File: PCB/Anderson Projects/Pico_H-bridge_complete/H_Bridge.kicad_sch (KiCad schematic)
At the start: 33 parts, among them Q1 AO3400A, Q2 AO3400A, Q3 DMP3130LQ-7, Q4 DMP3130LQ-7, U10 SN74LVC1G14DBV, U11 SN74LVC1G14DBV, U12 SN74LVC1G32, U13 SN74LVC1G32, U14 ILD217T, U15 ILD217T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

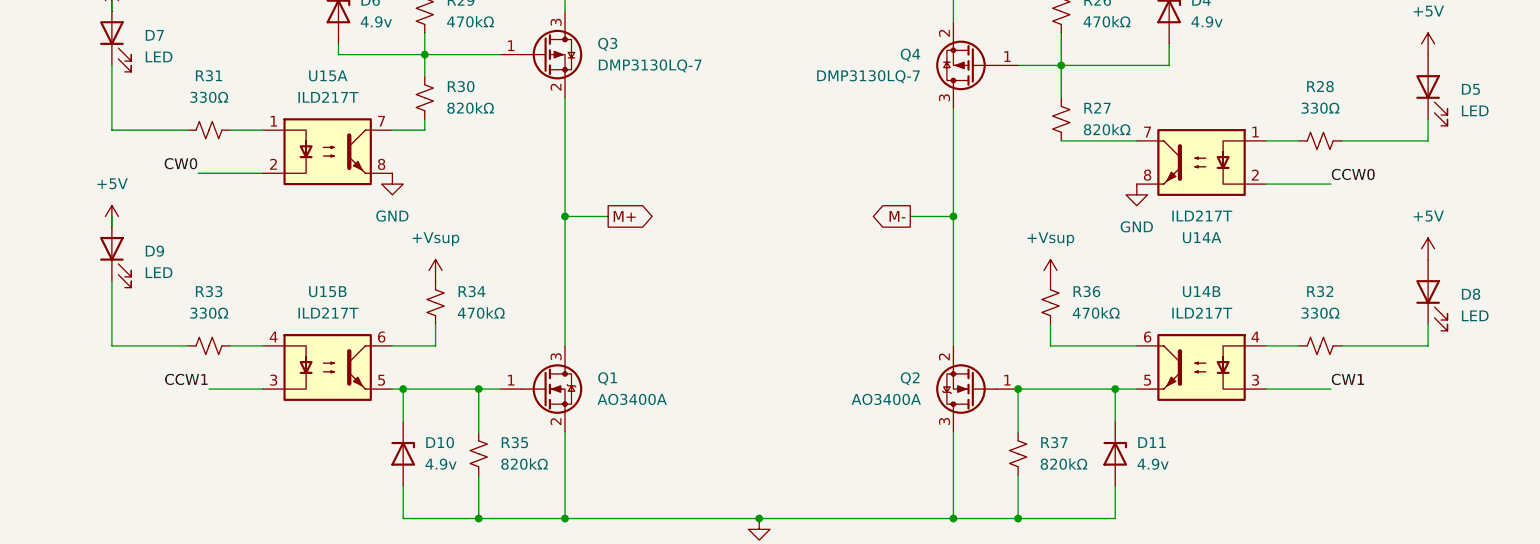
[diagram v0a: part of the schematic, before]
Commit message: Anderson Schematic with opto-couples prior to change to zener diodes
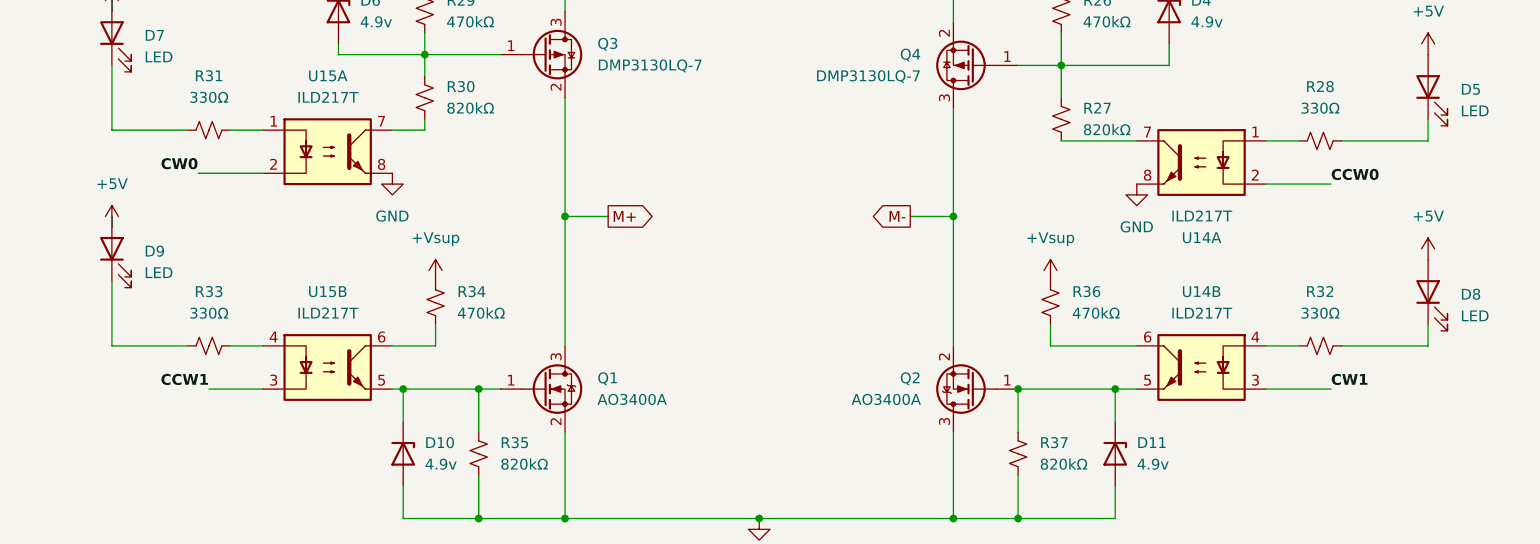
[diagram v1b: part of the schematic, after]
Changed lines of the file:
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@@
 			(font
 				(size 1.27 1.27)
+				(thickness 0.254)
+				(bold yes)
 			)
 			(justify left bottom)
@@
 			(font
 				(size 1.27 1.27)
+				(thickness 0.254)
+				(bold yes)
 			)
 			(justify left bottom)
@@
 			(font
 				(size 1.27 1.27)
+				(thickness 0.254)
+				(bold yes)
 			)
 			(justify right bottom)
@@
 			(font
 				(size 1.27 1.27)
+				(thickness 0.254)
+				(bold yes)
 			)
 			(justify right bottom)

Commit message: Changed Dig inputs  to zener buffers, removed all opto-couples, rebuilt h-bridge logic.
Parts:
- removed D4, D6: 4.9v, Diode_SMD:D_SOD-123, symbol Device:D_Zener
- removed R34, R36: 470kΩ, Resistor_SMD:R_0201_0603Metric, symbol Device:R_Small_US
- removed U11: SN74LVC1G14DBV, Package_TO_SOT_SMD:SOT-23-5, symbol 74xGxx:SN74LVC1G14DBV
- removed U14, U15: ILD217T, CustomBPA:SOIC-8_5.46mm_P1.27, symbol CustomBPA:ILD217T
- added Q5, Q6: MMBT3904, Package_TO_SOT_SMD:SOT-23, symbol Transistor_BJT:MMBT3904
- added U2, U3, U4: 74LVC1G08GV, Package_TO_SOT_SMD:SOT-23-5, symbol 74xGxx:74LVC1G08GV
- D5, D7, D8, D9: footprint LED_SMD:LED_0805_2012Metric -> C2297 - Green 0805
- R26, R29: value 470kΩ -> 10k
- R30: value 820kΩ -> 100Ω
- R31: value 330Ω -> 10k
- R32, R33: value 330Ω -> 100Ω
- R35, R37: value 820kΩ -> 10k
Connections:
- net +5V: now also U2.5 (VCC), U3.5 (VCC), U4.5 (VCC); no longer D5.2 (A), D7.2 (A), D8.2 (A), D9.2 (A)
- net CCW0: now also R27.2, U3.4; no longer U12.4
- net CCW1: now also R33.1, U12.4; no longer U12.1
- net CW0: now also R31.1, U2.4; no longer U13.4
- net CW1: now also R32.2, U13.4; no longer U10.4, U13.2
- net GND: now also D5.1 (K), D7.1 (K), D8.1 (K), D9.1 (K), Q5.2 (E), Q6.2 (E), U2.3 (GND), U3.3 (GND), U4.3 (GND); no longer R35.2, R37.2
- net S0: now also U9.1
- net at U13.1, U8.4: now also U2.1, U4.1
- net at Q3.1 (G), R29.2: now also R30.2; no longer R30.1
- net at Q4.1 (G), R26.2: now also R28.1; no longer R27.1
- net at D10.1 (K), Q1.1 (G), R35.1: now also R33.2
- net at R32.1: now also D11.1 (K), Q2.1 (G), R37.1
- net at R31.2: now also D7.2 (A), Q5.1 (B)
- net at R28.2: now also Q6.3 (C); no longer D5.1 (K)
- net at JP1.2 (C), U8.1: no longer U9.1
- net at U12.2, U9.4: now also U3.2, U4.2; no longer U10.2
- net Speed PWM renamed Speed_set PWM
- new net: Q5.3 (C), R30.1
- new net: D5.2 (A), Q6.1 (B), R27.1
- new net: D9.2 (A), R35.2
- new net: U10.2, U12.1, U13.2, U4.4
- new net: U10.4, U2.2, U3.1
- new net: D8.2 (A), R37.2
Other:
- moved on the sheet: D10, D11, D5, D7, D8, D9, JP1, Q1, Q2, Q3, Q4, R26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

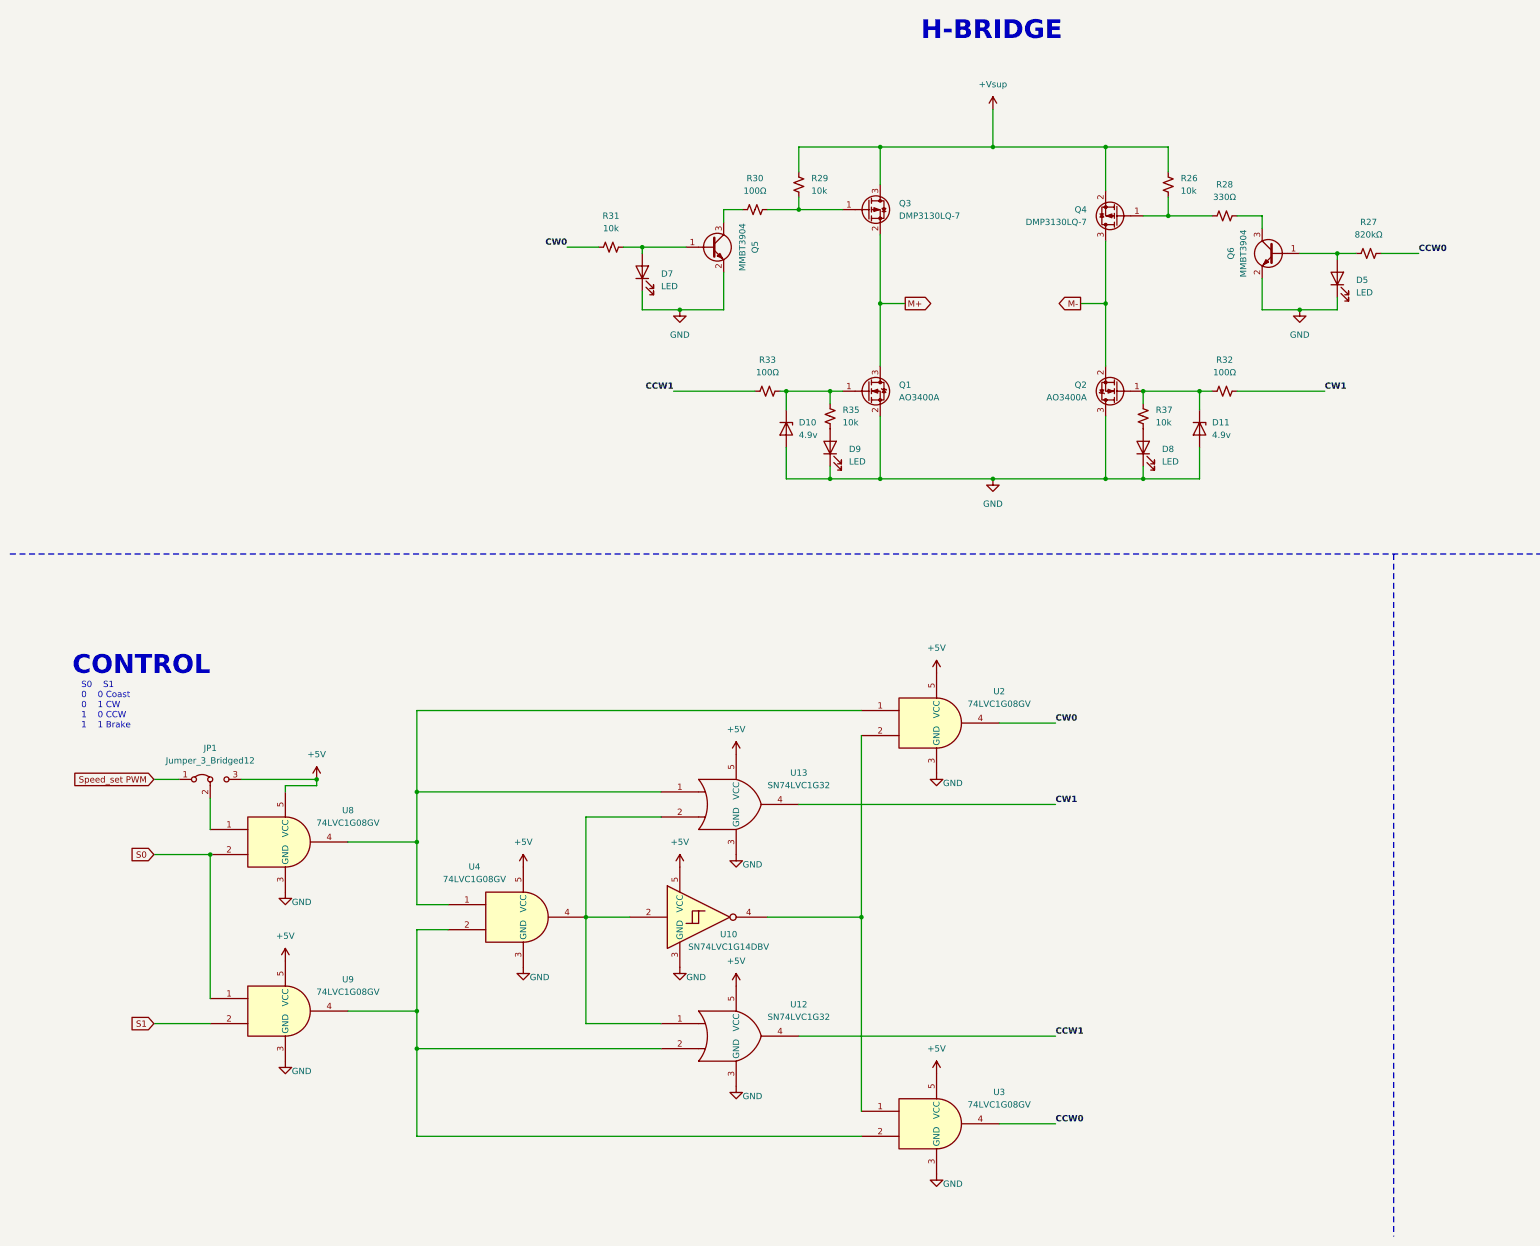
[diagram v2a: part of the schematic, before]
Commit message: Anderson PCB ready for board layout
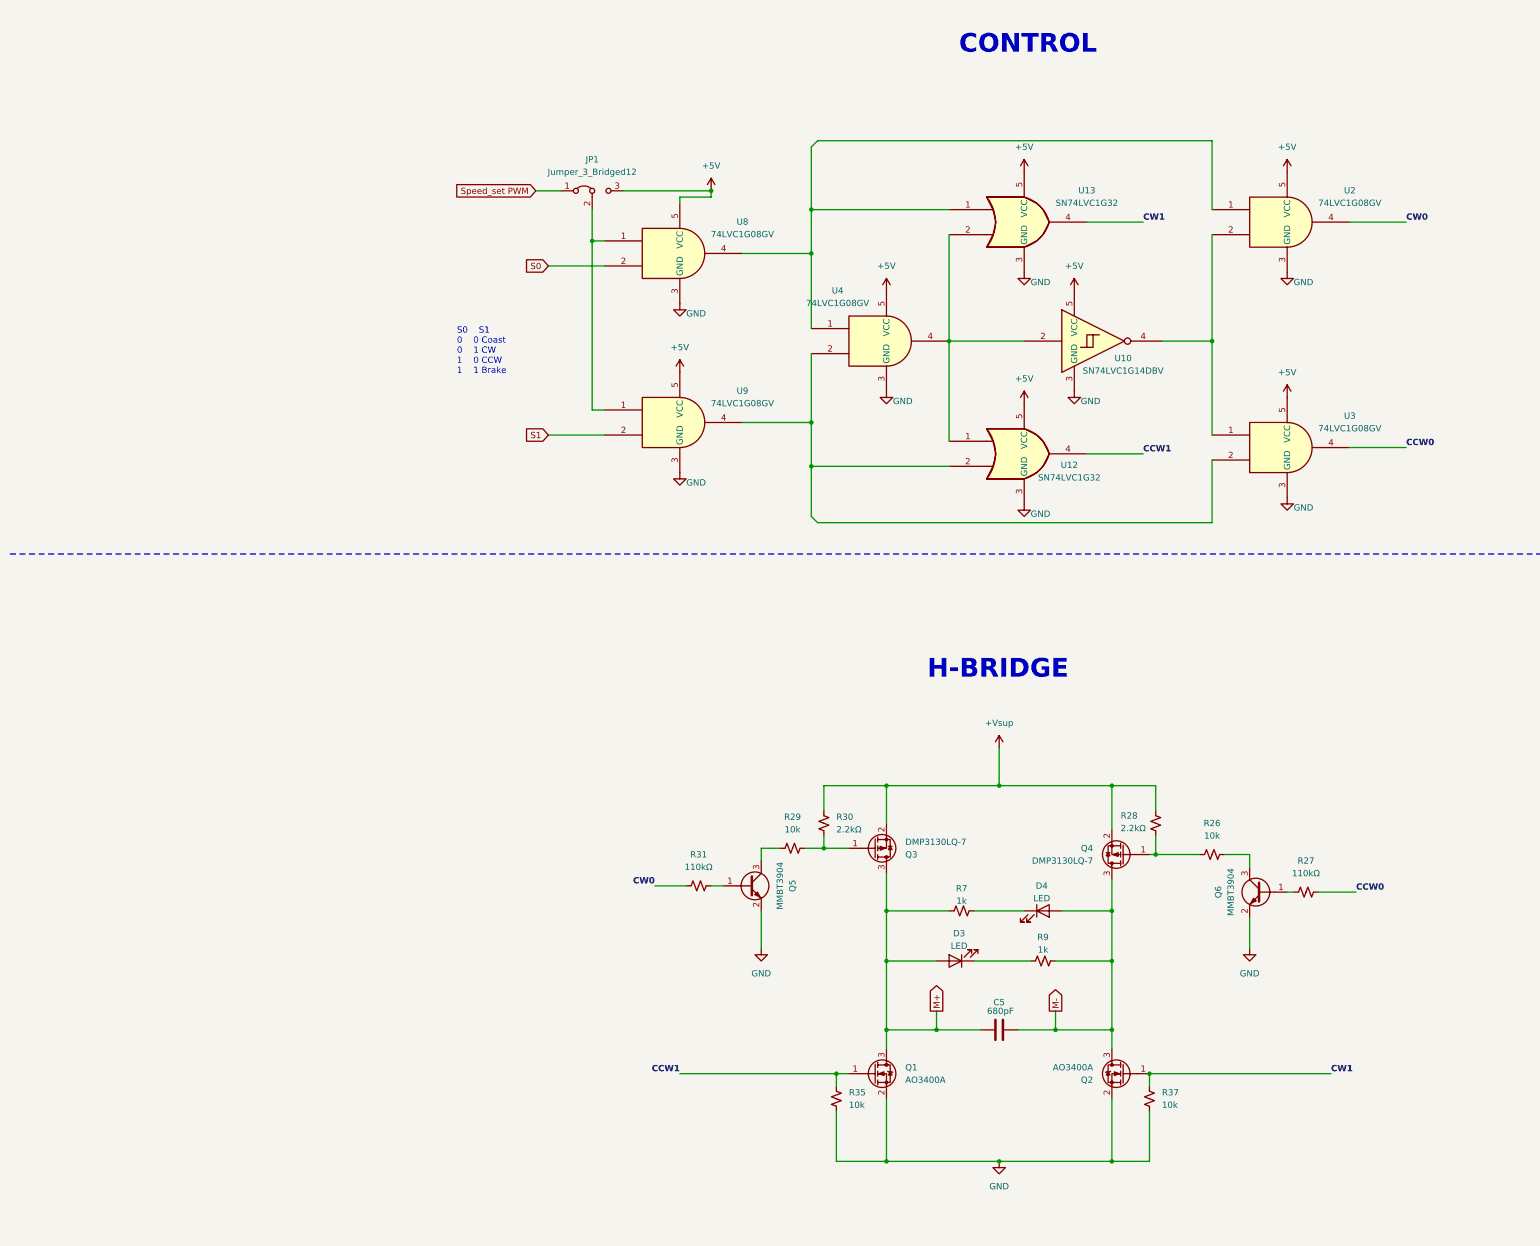
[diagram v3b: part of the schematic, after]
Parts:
- removed D10, D11: 4.9v, Diode_SMD:D_SOD-123, symbol Device:D_Zener
- removed D8, D9: LED, C2297 - Green 0805, symbol Device:LED
- removed R32, R33: 100Ω, Resistor_SMD:R_0201_0603Metric, symbol Device:R_Small_US
- added C5: 680pF, Capacitor_SMD:C_0603_1608Metric, symbol Device:C
- added R7, R9: 1k, Resistor_SMD:R_0603_1608Metric, symbol Device:R_Small_US
- D3: renamed from D5; footprint C2297 - Green 0805 -> LED_SMD:LED_0805_2012Metric
- D4: renamed from D7; footprint C2297 - Green 0805 -> LED_SMD:LED_0805_2012Metric
- Q3, Q4: symbol Transistor_FET:DMP3130LQ-7 -> CustomBPA:DMP3130LQ-7
- R26, R29, R35, R37: footprint Resistor_SMD:R_0201_0603Metric -> Resistor_SMD:R_0603_1608Metric
- R27: value 820kΩ -> 110kΩ; footprint Resistor_SMD:R_0201_0603Metric -> Resistor_SMD:R_0603_1608Metric
- R28: value 330Ω -> 2.2kΩ; footprint Resistor_SMD:R_0201_0603Metric -> Resistor_SMD:R_0603_1608Metric
- R30: value 100Ω -> 2.2kΩ; footprint Resistor_SMD:R_0201_0603Metric -> Resistor_SMD:R_0603_1608Metric
- R31: value 10k -> 110kΩ; footprint Resistor_SMD:R_0201_0603Metric -> Resistor_SMD:R_0603_1608Metric
- U12, U13: symbol 74xGxx:SN74LVC1G32 -> CustomBPA:SN74LVC1G32
- U2, U3, U4, U8, U9: symbol 74xGxx:74LVC1G08GV -> CustomBPA:74LVC1G08GV
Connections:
- net +Vsup: now also Q3.2 (S), R28.1, R30.2; no longer Q3.3 (D), R26.1, R29.1
- net CCW1: now also Q1.1 (G), R35.1
- net CW1: now also Q2.1 (G), R37.1
- net GND: now also Q2.2 (S), R35.2, R37.2; no longer D3.1 (K), D4.1 (K), Q2.3 (D)
- net M+: now also D3.2 (A), Q3.3 (D), C5.1, R7.2; no longer Q3.2 (S)
- net M-: now also D4.2 (A), Q2.3 (D), C5.2, R9.2; no longer Q2.2 (S)
- net S0: no longer U9.1
- net at Q5.1 (B), R31.2: no longer D4.2 (A)
- net at Q5.3 (C): now also R29.1; no longer R30.1
- net at Q3.1 (G), R29.2: now also R30.1; no longer R30.2
- net at Q6.1 (B), R27.1: no longer D3.2 (A)
- net at R28.2: now also Q4.1 (G), R26.1; no longer Q6.3 (C)
- net at JP1.2 (C), U8.1: now also U9.1
- new net: D4.1 (K), R7.1
- new net: Q6.3 (C), R26.2
- new net: D3.1 (K), R9.1
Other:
- moved on the sheet: D3, D4, JP1, Q1, Q2, Q3, Q4, Q5, Q6, R26, R27, R28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

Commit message: Anderson Pico_H-bridge_complete Gerbers ready to order
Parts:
- added TP10: CW0, TestPoint:TestPoint_Plated_Hole_D2.0mm, symbol Connector:TestPoint
- added TP11: CCW1, TestPoint:TestPoint_Plated_Hole_D2.0mm, symbol Connector:TestPoint
- added TP4: S0, TestPoint:TestPoint_Plated_Hole_D2.0mm, symbol Connector:TestPoint
- added TP5: S1, TestPoint:TestPoint_Plated_Hole_D2.0mm, symbol Connector:TestPoint
- added TP6: Q3, TestPoint:TestPoint_Plated_Hole_D2.0mm, symbol Connector:TestPoint
- added TP7: Q4, TestPoint:TestPoint_Plated_Hole_D2.0mm, symbol Connector:TestPoint
- added TP8: CCW0, TestPoint:TestPoint_Plated_Hole_D2.0mm, symbol Connector:TestPoint
- added TP9: CW1, TestPoint:TestPoint_Plated_Hole_D2.0mm, symbol Connector:TestPoint
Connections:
- net CCW0: now also TP8.1
- net CCW1: now also TP11.1
- net CW0: now also TP10.1
- net CW1: now also TP9.1
- net S0: now also TP4.1
- net S1: now also TP5.1
- net at Q3.1 (G), R29.2, R30.1: now also TP6.1
- net at Q4.1 (G), R26.1, R28.2: now also TP7.1

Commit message: minor edits prior to ordering, and assembly document creation
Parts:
- C5: LCSC (none) -> C1630
- D3, D4: value LED -> LED_G; LCSC (none) -> C2297
- Q1, Q2: LCSC (none) -> C20917
- Q3, Q4: LCSC (none) -> C461084
- Q5, Q6: LCSC (none) -> C20526
- R26, R29, R35, R37: LCSC (none) -> C25804
- R27, R31: LCSC (none) -> C25805
- R28, R30: LCSC (none) -> C4190
- R7, R9: LCSC (none) -> C21190
- U10: LCSC (none) -> C7835
- U12, U13: LCSC (none) -> C10096
- U2, U3, U4, U8, U9: LCSC (none) -> C19829591

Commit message: Updated Anderson Schematic to fix V0 issues
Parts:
- removed TP10: CW0, TestPoint:TestPoint_Plated_Hole_D2.0mm, symbol Connector:TestPoint
- removed TP11: CCW1, TestPoint:TestPoint_Plated_Hole_D2.0mm, symbol Connector:TestPoint
- removed TP6: Q3, TestPoint:TestPoint_Plated_Hole_D2.0mm, symbol Connector:TestPoint
- removed TP7: Q4, TestPoint:TestPoint_Plated_Hole_D2.0mm, symbol Connector:TestPoint
- removed TP8: CCW0, TestPoint:TestPoint_Plated_Hole_D2.0mm, symbol Connector:TestPoint
- removed TP9: CW1, TestPoint:TestPoint_Plated_Hole_D2.0mm, symbol Connector:TestPoint
- added C4, C8: 100uF, Capacitor_SMD:C_1210_3225Metric, symbol Device:C_Polarized_US
- added TP2: 10v, TestPoint:TestPoint_Plated_Hole_D2.0mm, symbol Connector:TestPoint
- added TP3: 5v, TestPoint:TestPoint_Plated_Hole_D2.0mm, symbol Connector:TestPoint
- added U6: LM7810, Package_TO_SOT_SMD:SOT-89-3, symbol Regulator_Linear:L78L10_SOT89
- added U7: LM78L05, Package_TO_SOT_SMD:SOT-89-3, symbol Regulator_Linear:LM78L05_TO92
- R7, R9: value 1k -> 2.7k; LCSC C21190 -> C13167
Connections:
- net +5V: now also TP3.1, U7.1 (VO)
- net +Vsup: now also C4.1, U6.3 (IN)
- net GND: now also C4.2, C8.2, U6.2 (GND), U7.2 (GND)
- net M-: now also R9.1; no longer R9.2
- net at D3.1 (K): now also R9.2; no longer R9.1
- new net +10V: C8.1, TP2.1, U6.1 (OUT), U7.3 (VI)
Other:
- note added: "Voltage Regulation NOTE: Place decouple near outputs of each"
- moved on the sheet: JP1, TP4, TP5, U10, U12, U13, U2, U3, U4, U8, U9
